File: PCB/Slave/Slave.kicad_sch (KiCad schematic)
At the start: 64 parts, among them J1 USB_C_Receptacle_USB2.0_16P, J2 Conn_01x05_Pin, J3 Conn_01x07_Socket, J4 Conn_01x04_Socket, J5 Conn_01x07_Socket, Q2 PNP, SW1 PTS810_SJM_250_SMTR_LFS, SW2 PTS810_SJM_250_SMTR_LFS, U1 ESP32-S3-MINI-1, U2 TCA9406DC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

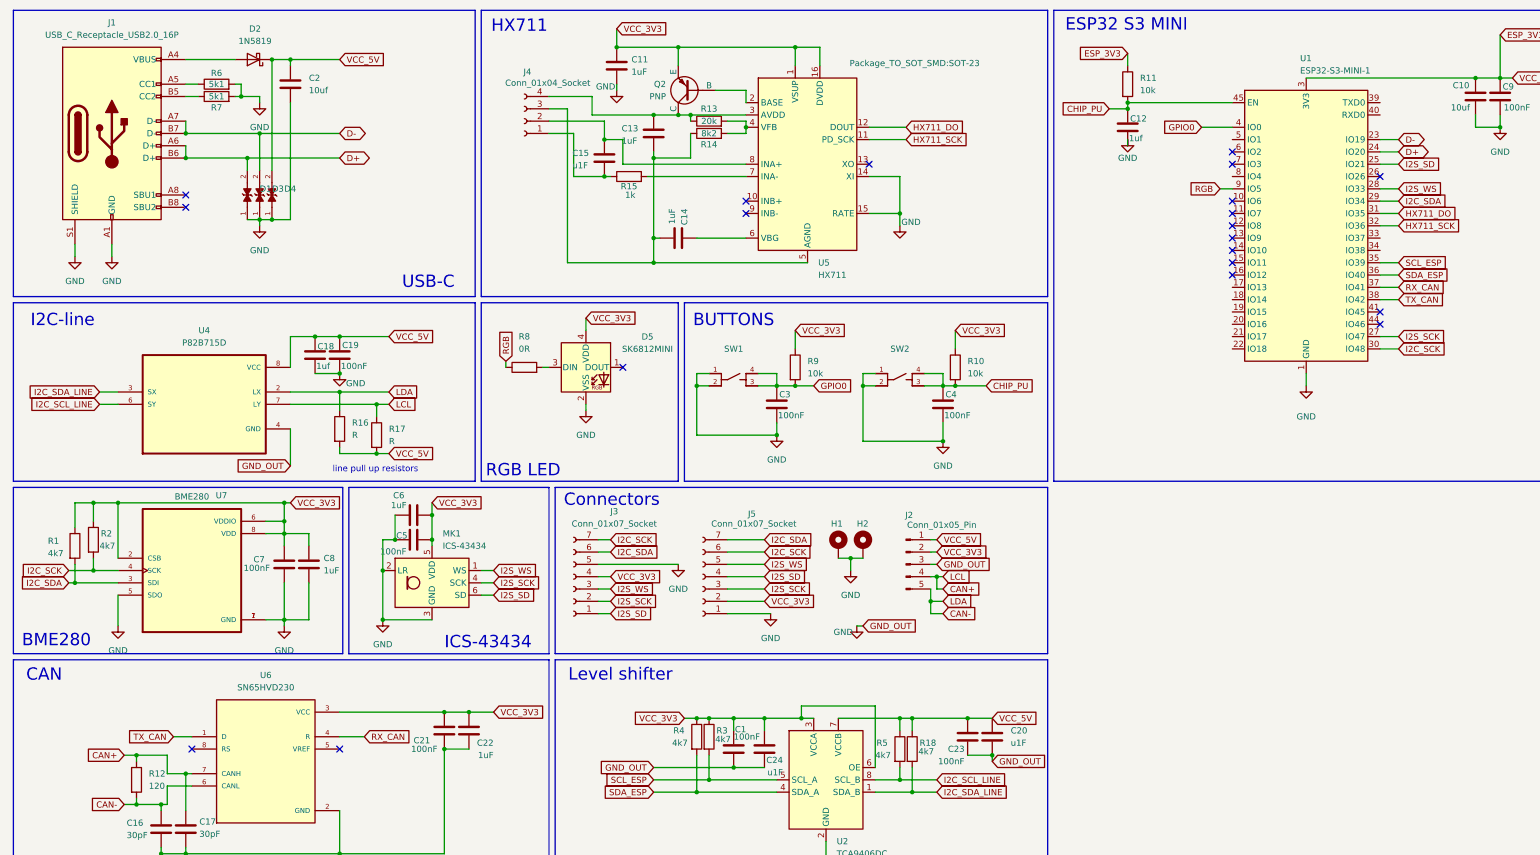
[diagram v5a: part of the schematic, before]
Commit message: repaired HX711
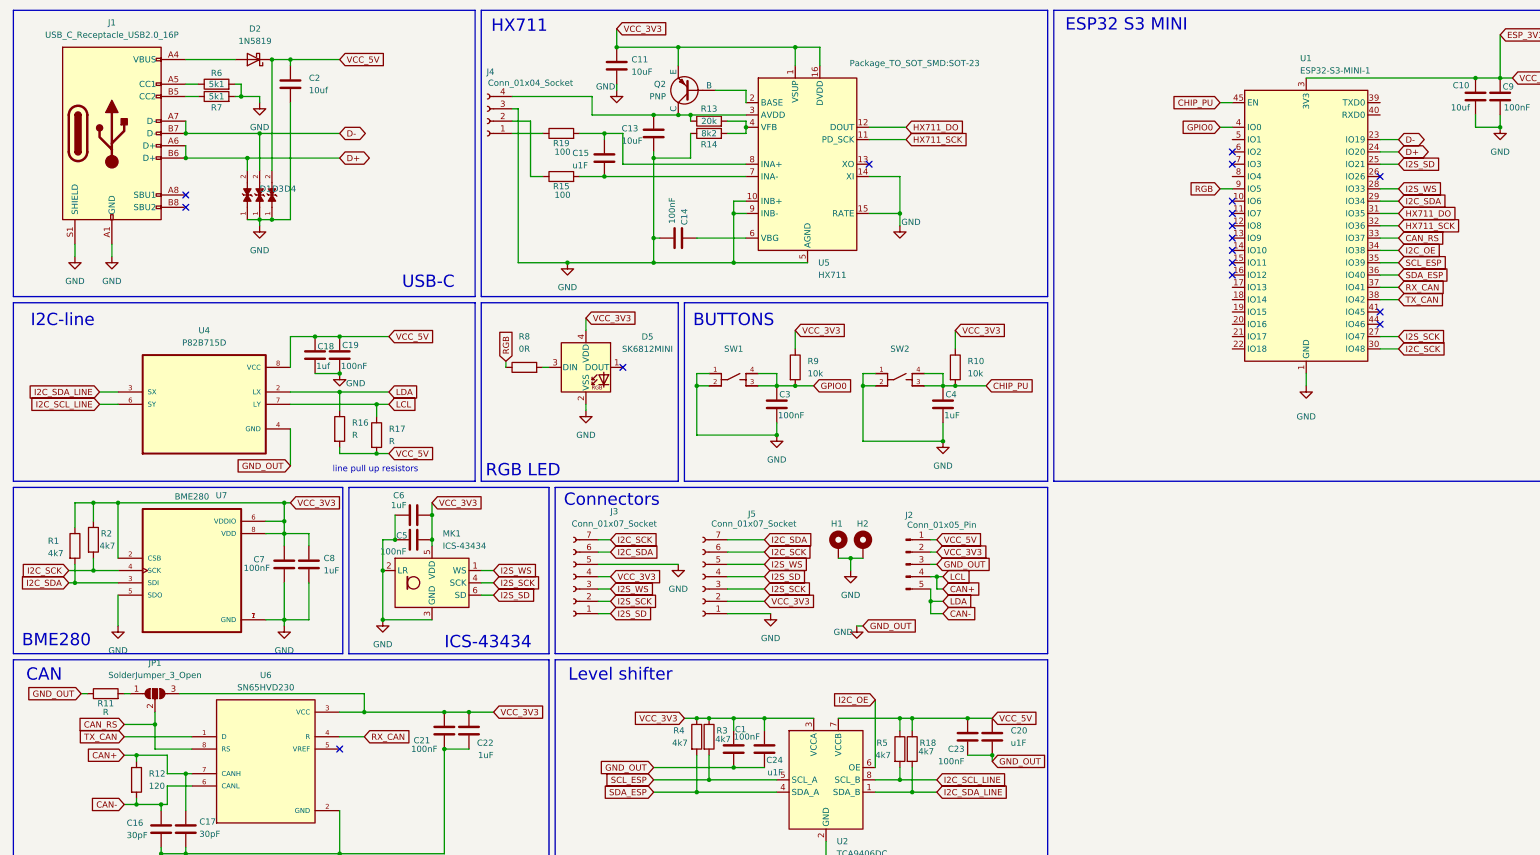
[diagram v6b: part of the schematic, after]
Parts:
- removed C12: 1uf, Capacitor_SMD:C_0603_1608Metric_Pad1.08x0.95mm_HandSolder, symbol Device:C
- added JP1: SolderJumper_3_Open, Jumper:SolderJumper-3_P1.3mm_Open_RoundedPad1.0x1.5mm, symbol Jumper:SolderJumper_3_Open
- added R19: 100, Resistor_SMD:R_0603_1608Metric_Pad0.98x0.95mm_HandSolder, symbol Device:R
- C11, C13: value 1uF -> 10uF
- C14: value 1uF -> 100nF
- C4: value 100nF -> 1uF
- R11: value 10k -> R
- R15: value 1k -> 100
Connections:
- net CHIP_PU: no longer R11.2
- net ESP_3V3: now also JP1.3 (B); no longer R11.1, U2.6 (OE)
- net GND: now also C13.2, C14.2, J4.3 (Pin_3), R11.1, R14.1, U5.10 (INB+), U5.5 (AGND), U5.9 (INB-)
- net at R15.2, U5.7 (INA-): now also C15.2
- net at C15.1, U5.8 (INA+): now also R19.2; no longer J4.2 (Pin_2)
- net CAN_RS: now reaches U6.8 (RS)
- net CAN_RS: now also U1.33 (IO37), JP1.2 (C)
- net I2C_OE: now reaches U1.34 (IO38)
- net I2C_OE: now also U2.6 (OE)
- new net: J4.1 (Pin_1), R19.1
- new net: J4.2 (Pin_2), R15.1
- new net: JP1.1 (A), R11.2
- no-connect marks 20 -> 17
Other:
- moved on the sheet: J4, R15

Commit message: Update_Prosinec
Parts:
- U1: footprint RF_Module:ESP32-S2-MINI-1 -> ESP32-S3-MINI-1-N8:XCVR_ESP32-S3-MINI-1-N8
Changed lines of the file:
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@@
 			)
 		)
-		(property "Footprint" "RF_Module:ESP32-S2-MINI-1"
+		(property "Footprint" "ESP32-S3-MINI-1-N8:XCVR_ESP32-S3-MINI-1-N8"
 			(at 294.64 87.63 0)
 			(effects

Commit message: SETUP FOR HANDOVER1
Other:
- note added: "BME280/ BME680"
- note removed: "BME280"
- title: (none) -> Příloha č.1 Schéma BEE modulu a sondy
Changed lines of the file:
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@@
 	(generator_version "8.0")
 	(paper "A3")
+	(title_block
+		(title "Příloha č.1 Schéma BEE modulu a sondy")
+		(date "2025-28-02")
+		(rev "Lukáš Vágner")
+	)
 	(junction
 		(at 170.18 91.44)
@@
 	(wire
 		(pts
+			(xy 88.9 140.97) (xy 88.9 139.7)
+		)
+		(stroke
+			(width 0)
+			(type default)
+		)
+	)
+	(wire
+		(pts
 			(xy 116.84 34.29) (xy 115.57 34.29)
 		)
@@
 		)
 	)
-	(text "BME280"
+	(text "BME280/\nBME680\n"
 		(exclude_from_sim no)
-		(at 21.59 144.018 0)
+		(at 22.352 142.748 0)
 		(effects
 			(font
@@
 		(dnp no)
 		(property "Reference" "C5"
-			(at 92.8385 122.3303 90)
+			(at 87.63 121.92 90)
 			(effects
 				(font
@@
 		)
 		(property "Value" "100nF"
-			(at 91.0605 125.6323 90)
+			(at 85.852 123.952 90)
 			(effects
 				(font
@@
 	(symbol
 		(lib_id "power:GND")
-		(at 88.9 139.7 0)
+		(at 88.9 140.97 0)
 		(unit 1)
 		(exclude_from_sim no)
@@
 		(on_board yes)
 		(dnp no)
-		(fields_autoplaced yes)
 		(property "Reference" "#PWR08"
-			(at 88.9 146.05 0)
+			(at 88.9 147.32 0)
 			(effects
 				(font
@@
 		)
 		(property "Value" "GND"
-			(at 88.9 144.78 0)
+			(at 88.9 145.542 0)
 			(effects
 				(font
@@
 		)
 		(property "Footprint" ""
-			(at 88.9 139.7 0)
+			(at 88.9 140.97 0)
 			(effects
 				(font
@@
 		)
 		(property "Datasheet" ""
-			(at 88.9 139.7 0)
+			(at 88.9 140.97 0)
 			(effects
 				(font
@@
 		)
 		(property "Description" "Power symbol creates a global label with name \"GND\" , ground"
-			(at 88.9 139.7 0)
+			(at 88.9 140.97 0)
 			(effects
 				(font
@@
 		(on_board yes)
 		(dnp no)
-		(fields_autoplaced yes)
 		(property "Reference" "#PWR022"
 			(at 68.58 147.32 0)
@@
 		)
 		(property "Value" "GND"
-			(at 68.58 146.05 0)
+			(at 68.58 145.542 0)
 			(effects
 				(font
@@
 		(on_board yes)
 		(dnp no)
-		(fields_autoplaced yes)
 		(property "Reference" "#PWR021"
 			(at 34.29 147.32 0)
@@
 		)
 		(property "Value" "GND"
-			(at 34.29 146.05 0)
+			(at 34.29 145.542 0)
 			(effects
 				(font
@@
 		(dnp no)
 		(property "Reference" "J4"
-			(at 111.125 26.67 0)
+			(at 110.998 28.956 0)
 			(effects
 				(font
@@
 					(size 1.27 1.27)
 				)
+				(hide yes)
 			)
 		)
@@
 					(size 1.27 1.27)
 				)
+				(hide yes)
 			)
 		)
